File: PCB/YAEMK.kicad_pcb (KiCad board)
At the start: 2 copper layers, 165.8 x 130.8 mm, 219 parts, among them J1 DBG, P1 PC, P2 Link, P3 SSD1107, Q1 MMUN2133LT1G, Q2 DMMT5401, Q3 AO3401A, SW1 ALPS EC11, U1 24LC64, U2 SSP6206, U3 USBLC6-2SC6, U4 USBLC6-2SC6, U5 STM32F303CCTx

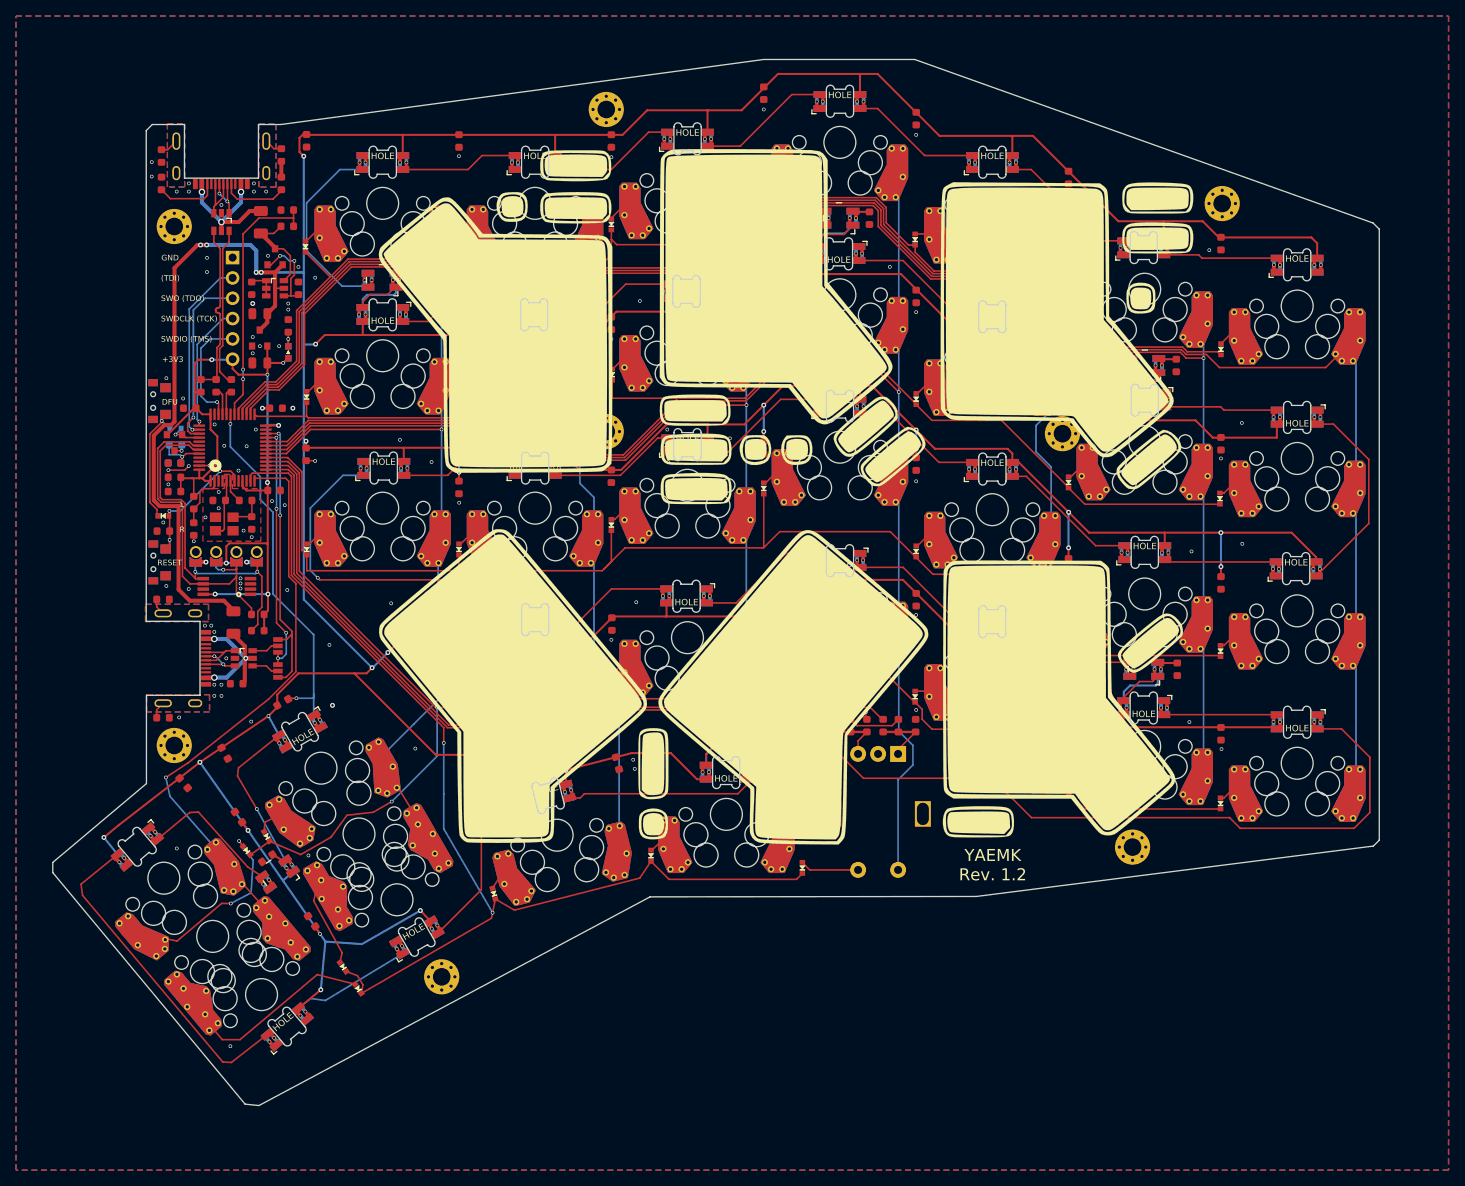
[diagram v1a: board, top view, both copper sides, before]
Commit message: Correct Diode Footprint add JLC assembly holes
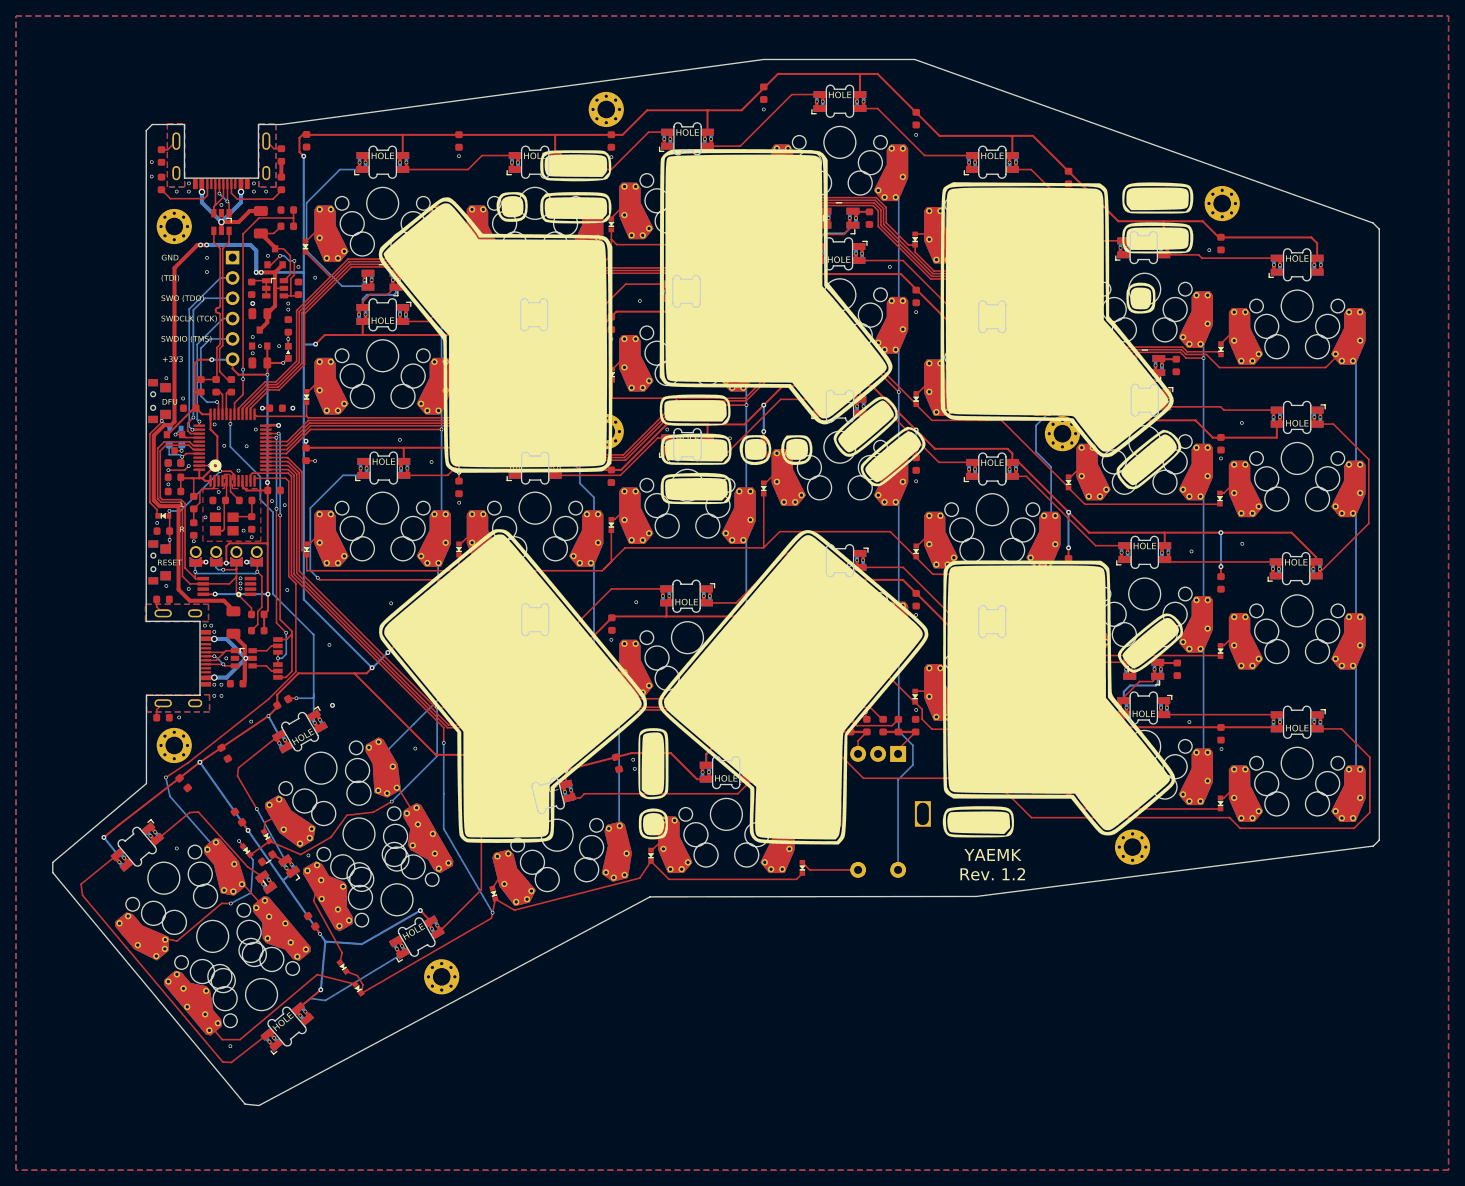
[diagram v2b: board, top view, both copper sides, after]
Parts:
- C46, C47: value 36p -> 12p
- D1, D10, D11, D12, D13, D14, D15, D16, D17, D18, D19, D2, D20, D21, D22, D23, D24, D25, D26, D27, D28, D29, D3, D30, D31, D32, D33, D34, D4, D5, D6, D7, D8, D9: value DIODE -> 1N4148
- R10, R9: value 5.1k -> 5k1
- R11: value 120 -> 220
- turned D1 to 130 degrees
- turned D10 to 90 degrees
- turned D11 to 90 degrees
- turned D12 to 105 degrees
- turned D13 to 90 degrees
- turned D14 to 90 degrees
- turned D15 to 90 degrees
- turned D16 to 90 degrees
- turned D17 to 90 degrees
- turned D18 to 90 degrees
- turned D19 to 90 degrees
- turned D2 to 125 degrees
- turned D20 to 90 degrees
- turned D21 to 90 degrees
- turned D22 to 90 degrees
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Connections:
- D1 pad 1: Net-(D1-Pad1) -> Row4
- D1 pad 2: Row4 -> Net-(D1-Pad2)
- D10 pad 1: Net-(D10-Pad1) -> Row3
- D10 pad 2: Row3 -> Net-(D10-Pad2)
- D11 pad 1: Net-(D11-Pad1) -> Row4
- D11 pad 2: Row4 -> Net-(D11-Pad2)
- D12 pad 1: Net-(D12-Pad1) -> Row5
- D12 pad 2: Row5 -> Net-(D12-Pad2)
- D13 pad 1: Net-(D13-Pad1) -> Row1
- D13 pad 2: Row1 -> Net-(D13-Pad2)
- D14 pad 1: Net-(D14-Pad1) -> Row2
- D14 pad 2: Row2 -> Net-(D14-Pad2)
- D15 pad 1: Net-(D15-Pad1) -> Row3
- D15 pad 2: Row3 -> Net-(D15-Pad2)
- D16 pad 1: Net-(D16-Pad1) -> Row4
- D16 pad 2: Row4 -> Net-(D16-Pad2)
- D17 pad 1: Net-(D17-Pad1) -> Row5
- D17 pad 2: Row5 -> Net-(D17-Pad2)
- D18 pad 1: Net-(D18-Pad1) -> Row1
- D18 pad 2: Row1 -> Net-(D18-Pad2)
- D19 pad 1: Net-(D19-Pad1) -> Row2
- D19 pad 2: Row2 -> Net-(D19-Pad2)
- D2 pad 1: Net-(D2-Pad1) -> Row5
- D2 pad 2: Row5 -> Net-(D2-Pad2)
- D20 pad 1: Net-(D20-Pad1) -> Row3
- D20 pad 2: Row3 -> Net-(D20-Pad2)
- D21 pad 1: Net-(D21-Pad1) -> Row4
- D21 pad 2: Row4 -> Net-(D21-Pad2)
- D22 pad 1: Rot_Row -> Row5
- D22 pad 2: Row5 -> Rot_Row
- D23 pad 1: Net-(D23-Pad1) -> Row1
- D23 pad 2: Row1 -> Net-(D23-Pad2)
- D24 pad 1: Net-(D24-Pad1) -> Row2
- D24 pad 2: Row2 -> Net-(D24-Pad2)
- D25 pad 1: Net-(D25-Pad1) -> Row3
- D25 pad 2: Row3 -> Net-(D25-Pad2)
- D26 pad 1: Net-(D26-Pad1) -> Row4
- D26 pad 2: Row4 -> Net-(D26-Pad2)
- D27 pad 1: Net-(D27-Pad1) -> Row1
- D27 pad 2: Row1 -> Net-(D27-Pad2)
- D28 pad 1: Net-(D28-Pad1) -> Row2
- D28 pad 2: Row2 -> Net-(D28-Pad2)
- D29 pad 1: Net-(D29-Pad1) -> Row3
- D29 pad 2: Row3 -> Net-(D29-Pad2)
- D3 pad 1: Net-(D3-Pad1) -> Row1
- D3 pad 2: Row1 -> Net-(D3-Pad2)
- D30 pad 1: Net-(D30-Pad1) -> Row4
- D30 pad 2: Row4 -> Net-(D30-Pad2)
- D31 pad 1: Net-(D31-Pad1) -> Row1
- D31 pad 2: Row1 -> Net-(D31-Pad2)
- D32 pad 1: Net-(D32-Pad1) -> Row2
- D32 pad 2: Row2 -> Net-(D32-Pad2)
- D33 pad 1: Net-(D33-Pad1) -> Row3
- D33 pad 2: Row3 -> Net-(D33-Pad2)
- D34 pad 1: Net-(D34-Pad1) -> Row4
- D34 pad 2: Row4 -> Net-(D34-Pad2)
- D4 pad 1: Net-(D4-Pad1) -> Row2
- D4 pad 2: Row2 -> Net-(D4-Pad2)
- D5 pad 1: Net-(D5-Pad1) -> Row3
- D5 pad 2: Row3 -> Net-(D5-Pad2)
- D6 pad 1: Net-(D6-Pad1) -> Row4
- D6 pad 2: Row4 -> Net-(D6-Pad2)
- D68 pad 1: BOOT0_CHARGE -> Net-(D68-Pad1)
- D68 pad 2: Net-(D68-Pad2) -> BOOT0_CHARGE
- D69 pad 1: NRST -> Net-(D68-Pad1)
- D69 pad 2: Net-(D68-Pad2) -> NRST
- D7 pad 1: Net-(D7-Pad1) -> Row5
- D7 pad 2: Row5 -> Net-(D7-Pad2)
- D8 pad 1: Net-(D8-Pad1) -> Row1
- D8 pad 2: Row1 -> Net-(D8-Pad2)
- D9 pad 1: Net-(D9-Pad1) -> Row2
- D9 pad 2: Row2 -> Net-(D9-Pad2)
- S1 pad B: Net-(D1-Pad1) -> Net-(D1-Pad2)
- S1 pad D: Net-(D2-Pad1) -> Net-(D2-Pad2)
- S10 pad 2: Net-(D12-Pad1) -> Net-(D12-Pad2)
- S11 pad 2: Net-(D13-Pad1) -> Net-(D13-Pad2)
- S12 pad 2: Net-(D14-Pad1) -> Net-(D14-Pad2)
- S13 pad 2: Net-(D15-Pad1) -> Net-(D15-Pad2)
- S14 pad 2: Net-(D16-Pad1) -> Net-(D16-Pad2)
- S15 pad 2: Net-(D17-Pad1) -> Net-(D17-Pad2)
- S16 pad 2: Net-(D18-Pad1) -> Net-(D18-Pad2)
- S17 pad 2: Net-(D19-Pad1) -> Net-(D19-Pad2)
- S18 pad 2: Net-(D20-Pad1) -> Net-(D20-Pad2)
- S19 pad 2: Net-(D21-Pad1) -> Net-(D21-Pad2)
- S2 pad 2: Net-(D3-Pad1) -> Net-(D3-Pad2)
- S20 pad 2: Net-(D23-Pad1) -> Net-(D23-Pad2)
- S21 pad 2: Net-(D24-Pad1) -> Net-(D24-Pad2)
- S22 pad 2: Net-(D25-Pad1) -> Net-(D25-Pad2)
- S23 pad 2: Net-(D26-Pad1) -> Net-(D26-Pad2)
- S24 pad 2: Net-(D27-Pad1) -> Net-(D27-Pad2)
- S25 pad 2: Net-(D28-Pad1) -> Net-(D28-Pad2)
- S26 pad 2: Net-(D29-Pad1) -> Net-(D29-Pad2)
- S27 pad 2: Net-(D30-Pad1) -> Net-(D30-Pad2)
- S28 pad 2: Net-(D31-Pad1) -> Net-(D31-Pad2)
- S29 pad 2: Net-(D32-Pad1) -> Net-(D32-Pad2)
- S3 pad 2: Net-(D4-Pad1) -> Net-(D4-Pad2)
- S30 pad 2: Net-(D33-Pad1) -> Net-(D33-Pad2)
- S31 pad 2: Net-(D34-Pad1) -> Net-(D34-Pad2)
- S32 pad 1: Net-(D68-Pad2) -> Net-(D68-Pad1)
- S4 pad 2: Net-(D5-Pad1) -> Net-(D5-Pad2)
- S5 pad B: Net-(D6-Pad1) -> Net-(D6-Pad2)
- S5 pad D: Net-(D7-Pad1) -> Net-(D7-Pad2)
- S6 pad 2: Net-(D8-Pad1) -> Net-(D8-Pad2)
- S7 pad 2: Net-(D9-Pad1) -> Net-(D9-Pad2)
- S8 pad 2: Net-(D10-Pad1) -> Net-(D10-Pad2)
- S9 pad 2: Net-(D11-Pad1) -> Net-(D11-Pad2)
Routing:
- net Net-(D2-Pad2): track 0.00 -> 27.8 mm
- net Net-(D2-Pad1): track 27.8 -> 0.00 mm
- net Net-(D1-Pad2): track 0.00 -> 26.2 mm, vias 0 -> 2
- net Net-(D1-Pad1): track 26.2 -> 0.00 mm, vias 2 -> 0
- net Net-(D68-Pad2): track 16.6 -> 0.00 mm, vias 1 -> 0
- net Net-(D68-Pad1): track 0.00 -> 16.6 mm, vias 0 -> 1
- net Net-(D7-Pad2): track 0.00 -> 11.2 mm
- net Net-(D7-Pad1): track 11.2 -> 0.00 mm
- net Net-(D21-Pad2): track 0.00 -> 6.24 mm
- net Net-(D21-Pad1): track 6.24 -> 0.00 mm
- net Net-(D34-Pad2): track 0.00 -> 4.93 mm
- net Net-(D34-Pad1): track 4.93 -> 0.00 mm
- net Net-(D5-Pad2): track 0.00 -> 4.52 mm
- net Net-(D5-Pad1): track 4.52 -> 0.00 mm
- net Net-(D17-Pad2): track 0.00 -> 3.96 mm
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
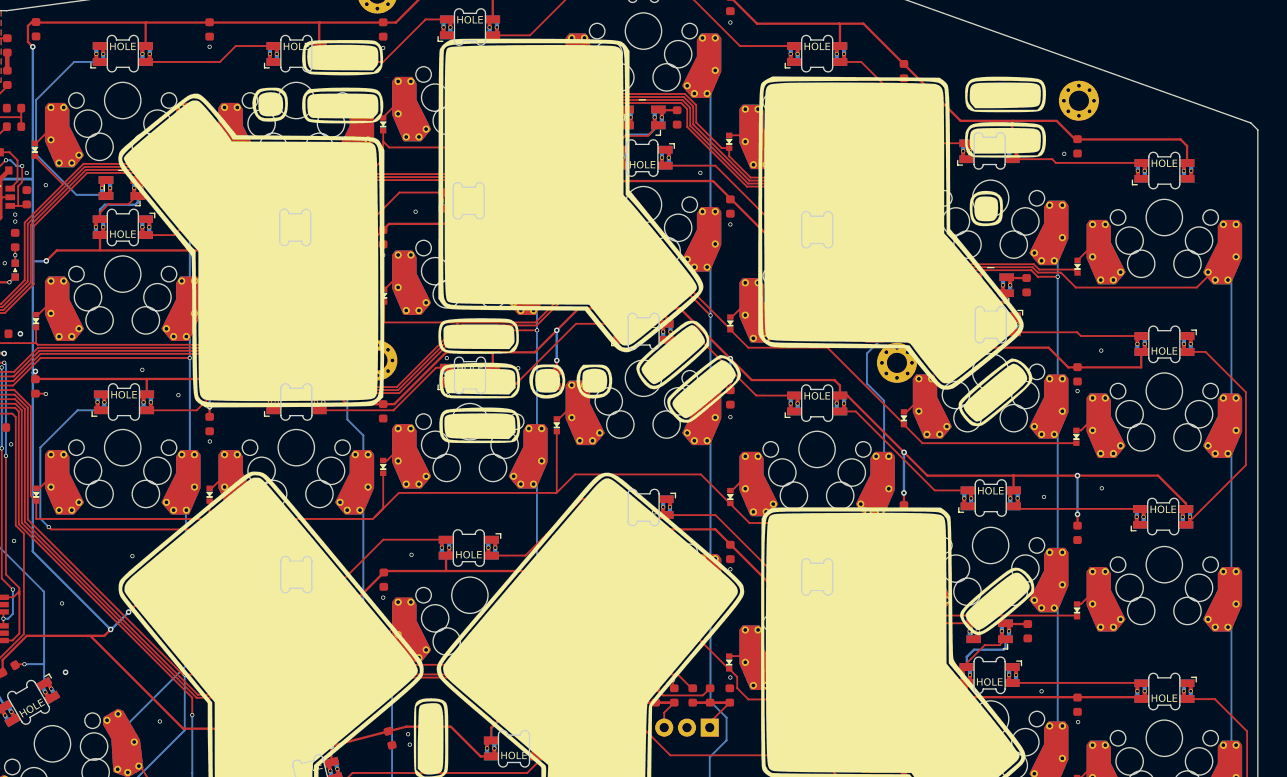
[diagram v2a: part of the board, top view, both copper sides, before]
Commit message: Add assembly holes for real
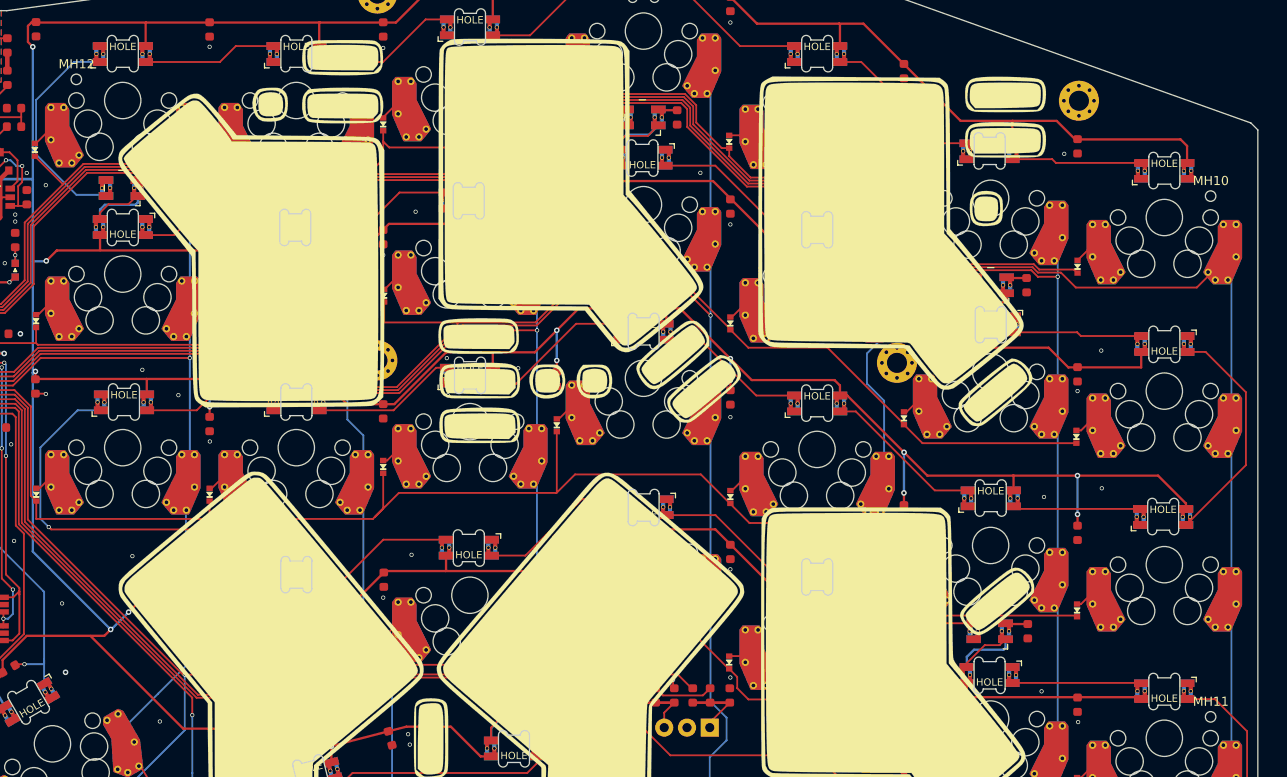
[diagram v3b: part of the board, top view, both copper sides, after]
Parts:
- added MH10: MOUNT_HOLE, prettylib:JLC_SMT_Assembly_Hole, F.Cu at (226.1, 53.7)
- added MH11: MOUNT_HOLE, prettylib:JLC_SMT_Assembly_Hole, F.Cu at (226.1, 110.9)
- added MH12: MOUNT_HOLE, prettylib:JLC_SMT_Assembly_Hole, F.Cu at (101.6, 40.9)
